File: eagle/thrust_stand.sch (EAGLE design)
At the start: 29 parts, among them IC1 7805TV, Q1 16Mhz, Q2 IRF510, SW1 EC12E_SW, T1 2N3904, U2 ATMEGA328P_PDIP

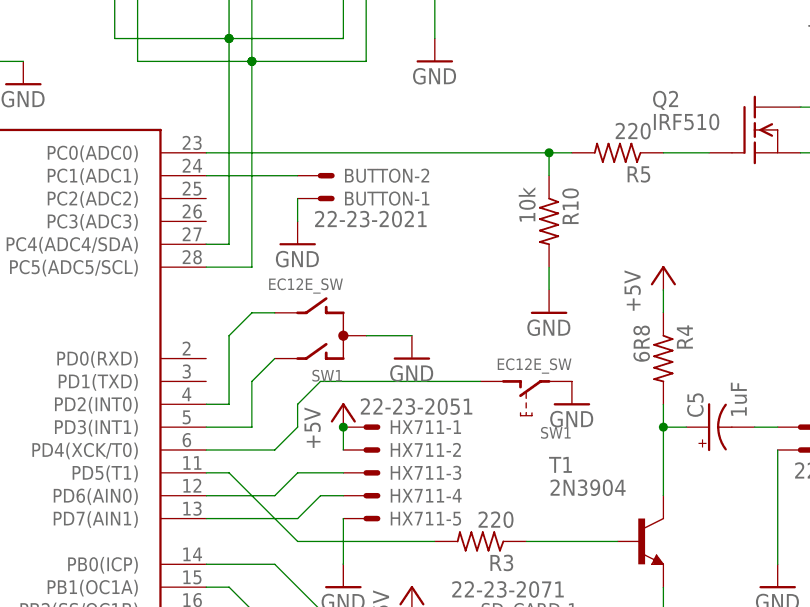
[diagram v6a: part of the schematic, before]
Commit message: routed with cutout
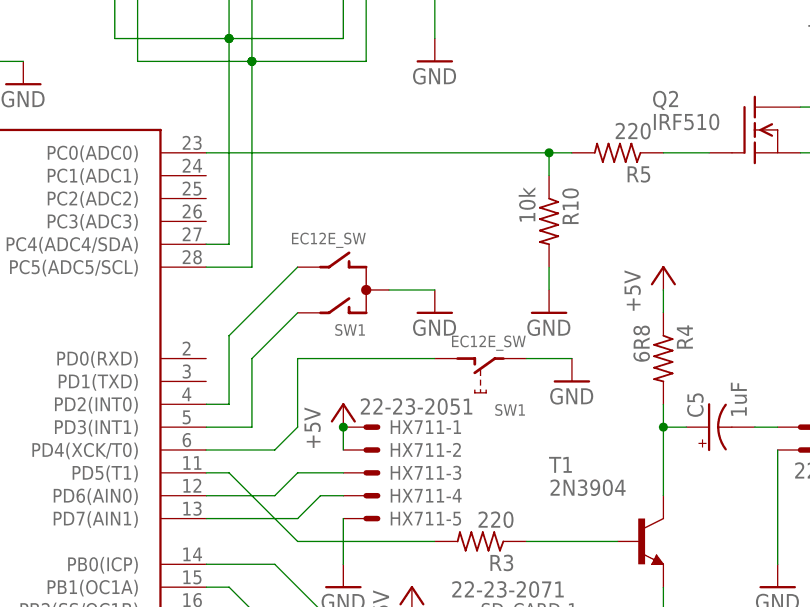
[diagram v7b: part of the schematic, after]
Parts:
- removed BUTTON: 22-23-2021, con-molex:22-23-2021
- R5: device rcl:R-US_0207/7 -> rcl:R-US_0309/10
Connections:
- removed net N$17: BUTTON-2.S, U2.PC1(ADC1)
- net GND: no longer BUTTON-1.S
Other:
- moved on the sheet: SW1
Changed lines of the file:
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@@
 <grid distance="0.1" unitdist="inch" unit="inch" style="lines" multiple="1" display="no" altdistance="0.01" altunitdist="inch" altunit="inch"/>
 <layers>
-<layer number="1" name="Top" color="4" fill="1" visible="no" active="no"/>
-<layer number="16" name="Bottom" color="1" fill="1" visible="no" active="no"/>
-<layer number="17" name="Pads" color="2" fill="1" visible="no" active="no"/>
-<layer number="18" name="Vias" color="2" fill="1" visible="no" active="no"/>
-<layer number="19" name="Unrouted" color="6" fill="1" visible="no" active="no"/>
-<layer number="20" name="Dimension" color="15" fill="1" visible="no" active="no"/>
-<layer number="21" name="tPlace" color="7" fill="1" visible="no" active="no"/>
-<layer number="22" name="bPlace" color="7" fill="1" visible="no" active="no"/>
-<layer number="23" name="tOrigins" color="15" fill="1" visible="no" active="no"/>
-<layer number="24" name="bOrigins" color="15" fill="1" visible="no" active="no"/>
-<layer number="25" name="tNames" color="7" fill="1" visible="no" active="no"/>
-<layer number="26" name="bNames" color="7" fill="1" visible="no" active="no"/>
-<layer number="27" name="tValues" color="7" fill="1" visible="no" active="no"/>
-<layer number="28" name="bValues" color="7" fill="1" visible="no" active="no"/>
+<layer number="1" name="Top" color="4" fill="1" visible="yes" active="no"/>
+<layer number="16" name="Bottom" color="1" fill="1" visible="yes" active="no"/>
+<layer number="17" name="Pads" color="2" fill="1" visible="yes" active="no"/>
+<layer number="18" name="Vias" color="2" fill="1" visible="yes" active="no"/>
+<layer number="19" name="Unrouted" color="6" fill="1" visible="yes" active="no"/>
+<layer number="20" name="Dimension" color="15" fill="1" visible="yes" active="no"/>
+<layer number="21" name="tPlace" color="7" fill="1" visible="yes" active="no"/>
+<layer number="22" name="bPlace" color="7" fill="1" visible="yes" active="no"/>
+<layer number="23" name="tOrigins" color="15" fill="1" visible="yes" active="no"/>
+<layer number="24" name="bOrigins" color="15" fill="1" visible="yes" active="no"/>
+<layer number="25" name="tNames" color="7" fill="1" visible="yes" active="no"/>
+<layer number="26" name="bNames" color="7" fill="1" visible="yes" active="no"/>
+<layer number="27" name="tValues" color="7" fill="1" visible="yes" active="no"/>
+<layer number="28" name="bValues" color="7" fill="1" visible="yes" active="no"/>
 <layer number="29" name="tStop" color="7" fill="3" visible="no" active="no"/>
 <layer number="30" name="bStop" color="7" fill="6" visible="no" active="no"/>
@@
 <layer number="35" name="tGlue" color="7" fill="4" visible="no" active="no"/>
 <layer number="36" name="bGlue" color="7" fill="5" visible="no" active="no"/>
-<layer number="37" name="tTest" color="7" fill="1" visible="no" active="no"/>
-<layer number="38" name="bTest" color="7" fill="1" visible="no" active="no"/>
+<layer number="37" name="tTest" color="7" fill="1" visible="yes" active="no"/>
+<layer number="38" name="bTest" color="7" fill="1" visible="yes" active="no"/>
 <layer number="39" name="tKeepout" color="4" fill="11" visible="no" active="no"/>
 <layer number="40" name="bKeepout" color="1" fill="11" visible="no" active="no"/>
@@
 <layer number="44" name="Drills" color="7" fill="1" visible="no" active="no"/>
 <layer number="45" name="Holes" color="7" fill="1" visible="no" active="no"/>
-<layer number="46" name="Milling" color="3" fill="1" visible="no" active="no"/>
-<layer number="47" name="Measures" color="7" fill="1" visible="no" active="no"/>
-<layer number="48" name="Document" color="7" fill="1" visible="no" active="no"/>
-<layer number="49" name="Reference" color="7" fill="1" visible="no" active="no"/>
-<layer number="50" name="dxf" color="7" fill="1" visible="no" active="no"/>
-<layer number="51" name="tDocu" color="7" fill="1" visible="no" active="no"/>
-<layer number="52" name="bDocu" color="7" fill="1" visible="no" active="no"/>
-<layer number="53" name="tGND_GNDA" color="7" fill="9" visible="no" active="no"/>
-<layer number="54" name="bGND_GNDA" color="1" fill="9" visible="no" active="no"/>
-<layer number="56" name="wert" color="7" fill="1" visible="no" active="no"/>
-<layer number="57" name="tCAD" color="7" fill="1" visible="no" active="no"/>
-<layer number="59" name="tCarbon" color="7" fill="1" visible="no" active="no"/>
-<layer number="60" name="bCarbon" color="7" fill="1" visible="no" active="no"/>
+<layer number="46" name="Milling" color="3" fill="1" visible="yes" active="no"/>
+<layer number="47" name="Measures" color="7" fill="1" visible="yes" active="no"/>
+<layer number="48" name="Document" color="7" fill="1" visible="yes" active="no"/>
+<layer number="49" name="Reference" color="7" fill="1" visible="yes" active="no"/>
+<layer number="50" name="dxf" color="7" fill="1" visible="yes" active="no"/>
+<layer number="51" name="tDocu" color="7" fill="1" visible="yes" active="no"/>
+<layer number="52" name="bDocu" color="7" fill="1" visible="yes" active="no"/>
+<layer number="53" name="tGND_GNDA" color="7" fill="9" visible="yes" active="no"/>
+<layer number="54" name="bGND_GNDA" color="1" fill="9" visible="yes" active="no"/>
+<layer number="56" name="wert" color="7" fill="1" visible="yes" active="no"/>
+<layer number="57" name="tCAD" color="7" fill="1" visible="yes" active="no"/>
+<layer number="59" name="tCarbon" color="7" fill="1" visible="yes" active="no"/>
+<layer number="60" name="bCarbon" color="7" fill="1" visible="yes" active="no"/>
 <layer number="90" name="Modules" color="5" fill="1" visible="yes" active="yes"/>
 <layer number="91" name="Nets" color="2" fill="1" visible="yes" active="yes"/>
@@
 <part name="BATTERY" library="con-molex" deviceset="22-23-2021" device=""/>
 <part name="GND9" library="supply1" deviceset="GND" device=""/>
-<part name="R5" library="rcl" deviceset="R-US_" device="0207/7" value="220"/>
+<part name="R5" library="rcl" deviceset="R-US_" device="0309/10" value="220"/>
 <part name="R10" library="rcl" deviceset="R-US_" device="0207/7" value="10k"/>
 <part name="GND5" library="supply1" deviceset="GND" device=""/>
@@
 <part name="GND7" library="supply1" deviceset="GND" device=""/>
 <part name="GND10" library="supply1" deviceset="GND" device=""/>
-<part name="BUTTON" library="con-molex" deviceset="22-23-2021" device=""/>
-<part name="GND11" library="supply1" deviceset="GND" device=""/>
 <part name="IGNITER" library="testpad" deviceset="PTR2" device=""/>
 <part name="SW1" library="switch-alps" deviceset="EC12E_SW" device=""/>
@@
 <instance part="GND7" gate="1" x="91.44" y="17.78"/>
 <instance part="GND10" gate="1" x="104.14" y="25.4"/>
-<instance part="BUTTON" gate="-1" x="53.34" y="68.58" rot="MR180"/>
-<instance part="BUTTON" gate="-2" x="53.34" y="71.12" rot="MR180"/>
-<instance part="GND11" gate="1" x="50.8" y="63.5"/>
 <instance part="IGNITER" gate="-1" x="116.84" y="66.04" rot="R90"/>
 <instance part="IGNITER" gate="-2" x="137.16" y="66.04" rot="R270"/>
-<instance part="SW1" gate="G$1" x="55.88" y="53.34" rot="R90"/>
-<instance part="SW1" gate="G$2" x="76.2" y="48.26" rot="R180"/>
-<instance part="GND12" gate="1" x="63.5" y="50.8"/>
-<instance part="GND13" gate="1" x="81.28" y="45.72"/>
+<instance part="SW1" gate="G$1" x="58.42" y="58.42" rot="R90"/>
+<instance part="SW1" gate="G$2" x="71.12" y="50.8" rot="R180"/>
+<instance part="GND12" gate="1" x="66.04" y="55.88"/>
+<instance part="GND13" gate="1" x="81.28" y="48.26"/>
 </instances>
 <busses>
@@
 </segment>
 <segment>
-<pinref part="GND11" gate="1" pin="GND"/>
-<pinref part="BUTTON" gate="-1" pin="S"/>
-<wire x1="50.8" y1="66.04" x2="50.8" y2="68.58" width="0.1524" layer="91"/>
-</segment>
-<segment>
 <pinref part="SW1" gate="G$1" pin="C"/>
 <pinref part="GND12" gate="1" pin="GND"/>
-<wire x1="58.42" y1="53.34" x2="63.5" y2="53.34" width="0.1524" layer="91"/>
+<wire x1="60.96" y1="58.42" x2="66.04" y2="58.42" width="0.1524" layer="91"/>
 </segment>
 <segment>
 <pinref part="SW1" gate="G$2" pin="2"/>
 <pinref part="GND13" gate="1" pin="GND"/>
+<wire x1="76.2" y1="50.8" x2="81.28" y2="50.8" width="0.1524" layer="91"/>
 </segment>
 </net>
@@
 </segment>
 </net>
-<net name="N$17" class="0">
-<segment>
-<pinref part="BUTTON" gate="-2" pin="S"/>
-<pinref part="U2" gate="G$1" pin="PC1(ADC1)"/>
-<wire x1="50.8" y1="71.12" x2="40.64" y2="71.12" width="0.1524" layer="91"/>
-</segment>
-</net>
 <net name="N$13" class="0">
 <segment>
@@
 <wire x1="40.64" y1="45.72" x2="43.18" y2="45.72" width="0.1524" layer="91"/>
 <wire x1="43.18" y1="45.72" x2="43.18" y2="53.34" width="0.1524" layer="91"/>
-<wire x1="43.18" y1="53.34" x2="45.72" y2="55.88" width="0.1524" layer="91"/>
 <pinref part="SW1" gate="G$1" pin="B"/>
-<wire x1="45.72" y1="55.88" x2="48.26" y2="55.88" width="0.1524" layer="91"/>
+<wire x1="43.18" y1="53.34" x2="50.8" y2="60.96" width="0.1524" layer="91"/>
 </segment>
 </net>
@@
 <wire x1="40.64" y1="43.18" x2="45.72" y2="43.18" width="0.1524" layer="91"/>
 <pinref part="SW1" gate="G$1" pin="A"/>
-<wire x1="45.72" y1="43.18" x2="45.72" y2="48.26" width="0.1524" layer="91"/>
-<wire x1="45.72" y1="48.26" x2="48.26" y2="50.8" width="0.1524" layer="91"/>
+<wire x1="45.72" y1="43.18" x2="45.72" y2="50.8" width="0.1524" layer="91"/>
+<wire x1="45.72" y1="50.8" x2="50.8" y2="55.88" width="0.1524" layer="91"/>
 </segment>
 </net>
@@
 <wire x1="40.64" y1="40.64" x2="48.26" y2="40.64" width="0.1524" layer="91"/>
 <wire x1="48.26" y1="40.64" x2="50.8" y2="43.18" width="0.1524" layer="91"/>
-<wire x1="50.8" y1="43.18" x2="50.8" y2="45.72" width="0.1524" layer="91"/>
-<wire x1="50.8" y1="45.72" x2="53.34" y2="48.26" width="0.1524" layer="91"/>
+<wire x1="50.8" y1="43.18" x2="50.8" y2="50.8" width="0.1524" layer="91"/>
 <pinref part="SW1" gate="G$2" pin="1"/>
-<wire x1="53.34" y1="48.26" x2="71.12" y2="48.26" width="0.1524" layer="91"/>
-</segment>
-</net>
+<wire x1="50.8" y1="50.8" x2="66.04" y2="50.8" width="0.1524" layer="91"/>
+</segment>
+</net>
